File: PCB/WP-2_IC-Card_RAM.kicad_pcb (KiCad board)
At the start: 2 copper layers, 54 x 54 mm, 11 parts, among them J1 Conn_01x38_Female, U1 628128_TSOP-I-32

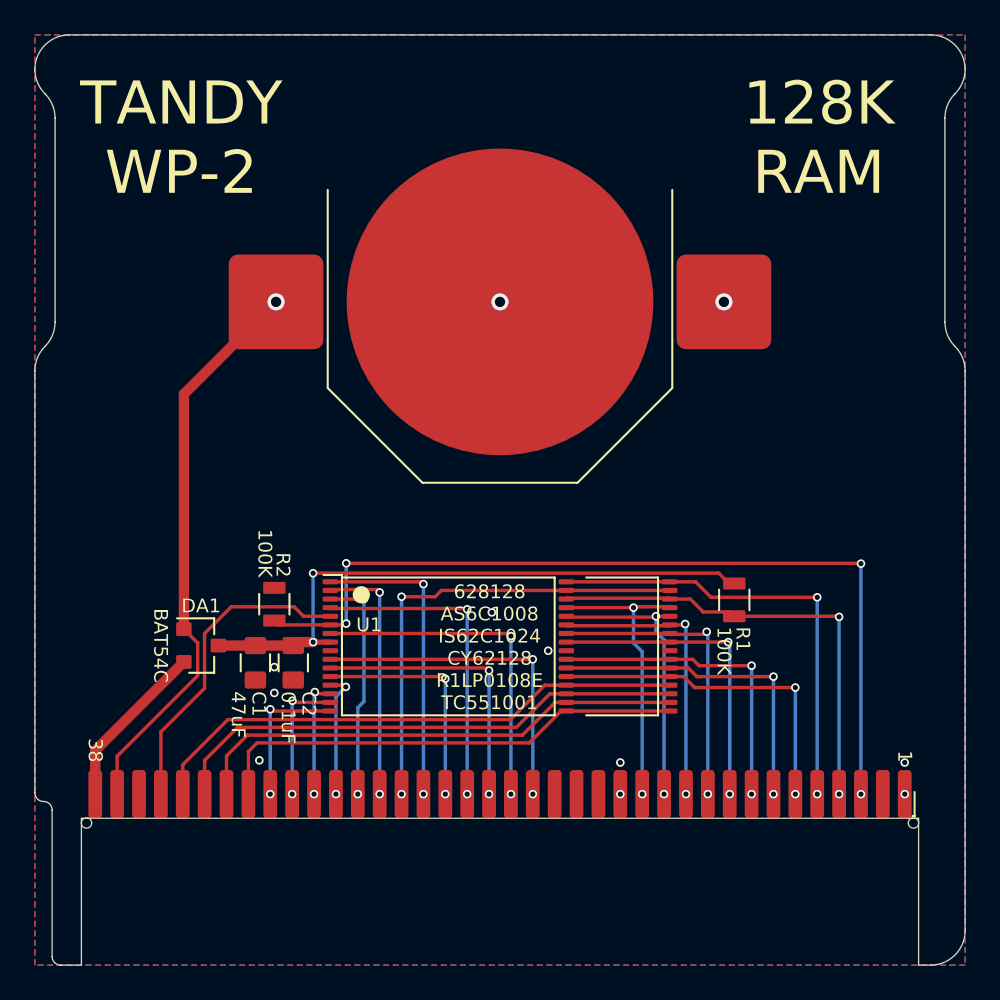
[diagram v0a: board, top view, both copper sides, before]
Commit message: simpler caps for ram card, 3d-printed cover, new WIP 4-bank MRAM card
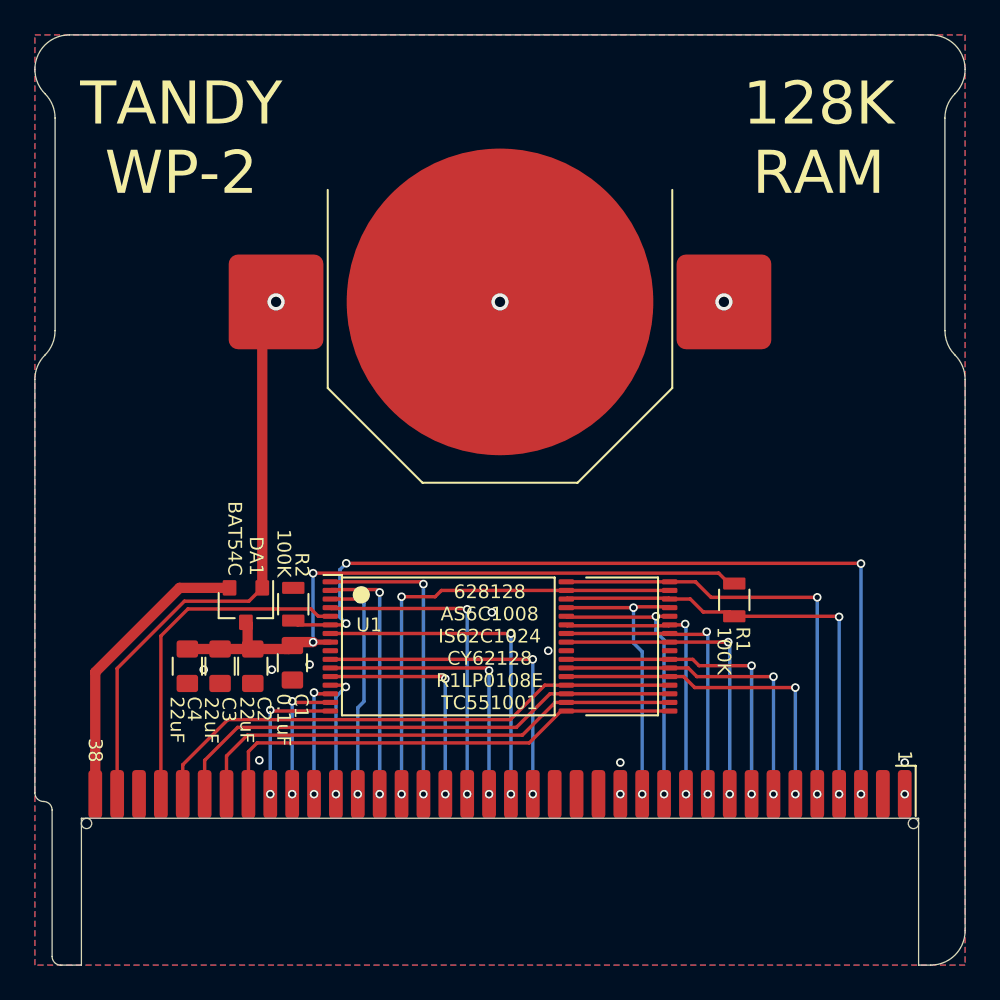
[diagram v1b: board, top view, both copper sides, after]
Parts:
- added C3: 22uF, 0_LOCAL:C_0805_1mm, F.Cu at (119.7, 104.9)
- added C4: 22uF, 0_LOCAL:C_0805_1mm, F.Cu at (117.8, 104.9)
- C1: value 47uF -> 0.1uF; footprint 0_LOCAL:C_0805 -> 0_LOCAL:C_0805_1mm
- C2: value 0.1uF -> 22uF; footprint 0_LOCAL:C_0805 -> 0_LOCAL:C_0805_1mm
- U1: value 628128_TSOP-I-32 -> 628128_TSOP
- moved DA1 3.50 mm to (121.2, 101.3), turned to -90 degrees
- moved C2 2.36 mm to (121.6, 104.9)
- moved C1 2.15 mm to (123.9, 104.7)
- moved R2 1.10 mm to (124.0, 101.3)
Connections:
- net /VMEM renamed VMEM
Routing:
- net /VBUS: track 9.33 -> 16.4 mm
- net VMEM: track 35.3 -> 38.9 mm
- net /VBAT: track 33.1 -> 34.6 mm
- net /~{WE}: track 18.5 -> 19.8 mm
- net /CE2: track 51.1 -> 50.3 mm
- net GND: vias 10 -> 11
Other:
- outline, holes or cut-outs redrawn
- board text added: "Battery: CR2016"
- board text removed: "Battery: CR2016 2 minutes grace period to change battery"

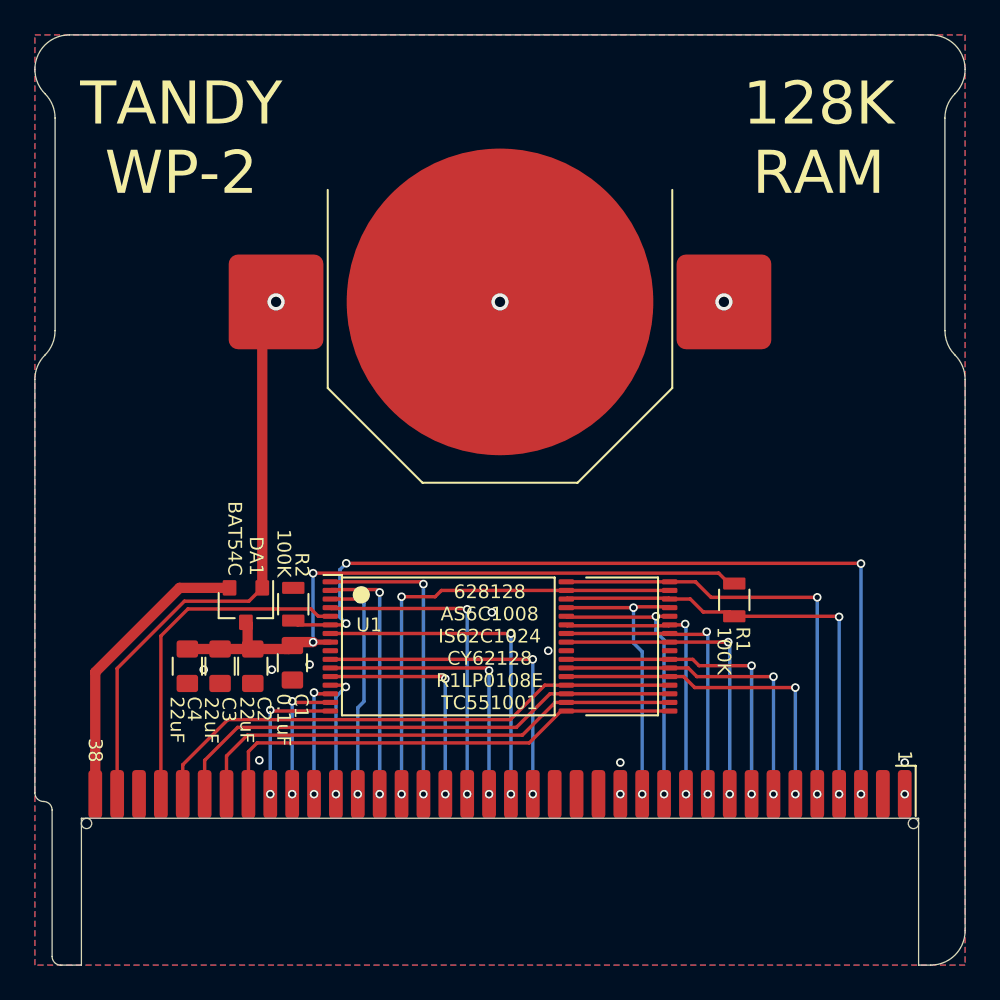
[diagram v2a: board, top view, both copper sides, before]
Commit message: MRAM level shifters, delete FRAM, local datasheets in local symbols
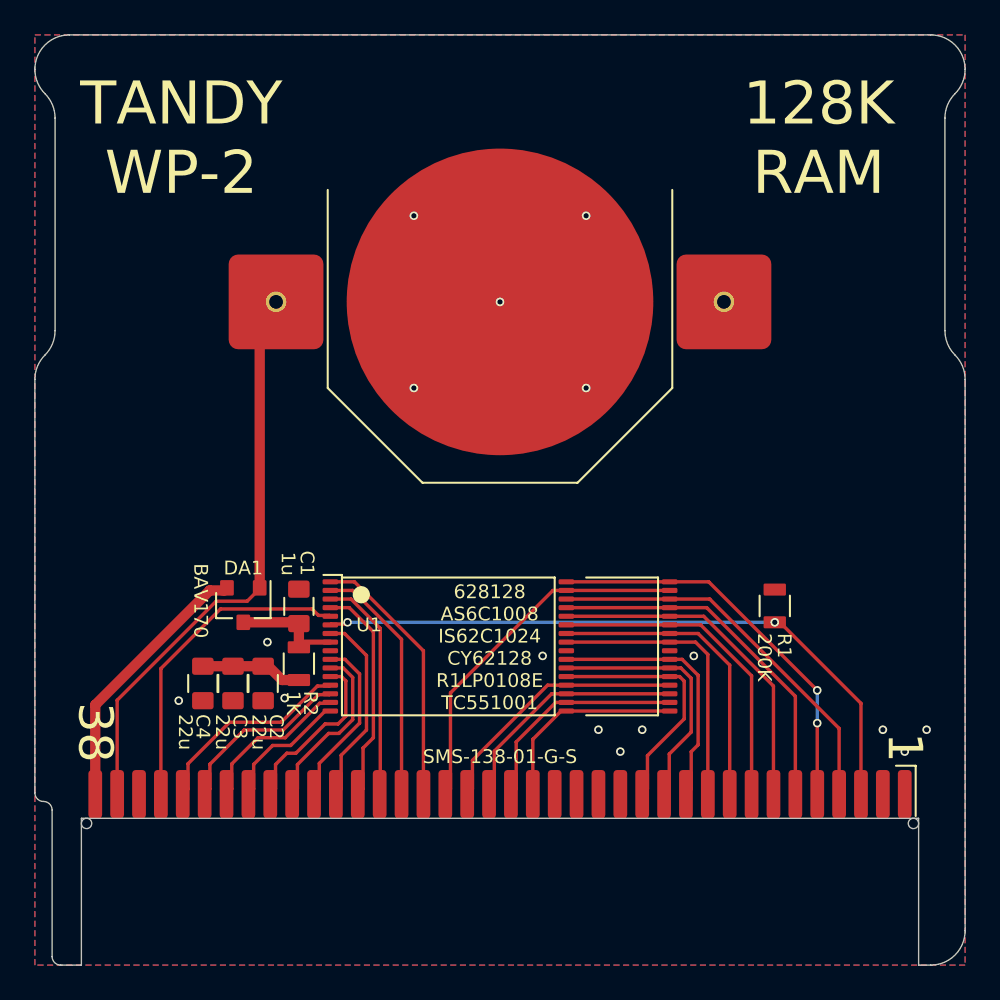
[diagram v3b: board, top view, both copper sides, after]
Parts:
- removed the R1 at (149.6, 101.0)
- added R2: 1K, 0_LOCAL:R_0805, F.Cu at (124.3, 104.7)
- added nail1: pth_nail, 0_LOCAL:pth_nail, F.Cu at (123.0, 83.7)
- added nail2: pth_nail, 0_LOCAL:pth_nail, F.Cu at (148.9, 83.7)
- C1: value 0.1uF -> 1u
- C2, C3, C4: value 22uF -> 22u
- DA1: value BAT54C -> BAV170
- J1: value Conn_01x38_Female -> SMS-138-01-G-S
- R1: renamed from R2; value 100K -> 200K
- moved R1 28.0 mm to (151.9, 101.4)
- moved C1 3.30 mm to (124.3, 101.4), turned to 90 degrees
- moved C4 1.35 mm to (118.7, 105.9)
- moved C3 1.25 mm to (120.5, 105.9)
- moved C2 1.17 mm to (122.2, 105.9)
- moved DA1 0.15 mm to (121.0, 101.3)
- renumbered REF** to corner1, REF** to corner2
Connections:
- C2 pad 1: VMEM -> Net-(C2-Pad1)
- C3 pad 1: VMEM -> Net-(C2-Pad1)
- C4 pad 1: VMEM -> Net-(C2-Pad1)
- U1 pad 10: /A16 -> /A6
- U1 pad 11: /A14 -> /A5
- U1 pad 12: /A12 -> /A4
- U1 pad 13: /A7 -> /A0
- U1 pad 14: /A6 -> /A1
- U1 pad 15: /A5 -> /A2
- U1 pad 16: /A4 -> /A3
- U1 pad 17: /A3 -> /A16
- U1 pad 18: /A2 -> /A15
- U1 pad 19: /A1 -> /A14
- U1 pad 2: /A9 -> /A10
- U1 pad 20: /A0 -> /A13
- U1 pad 21: /D0 -> /D7
- U1 pad 22: /D1 -> /D6
- U1 pad 23: /D2 -> /D5
- U1 pad 25: /D3 -> /D4
- U1 pad 26: /D4 -> /D3
- U1 pad 27: /D5 -> /D2
- U1 pad 28: /D6 -> /D1
- U1 pad 29: /D7 -> /D0
- U1 pad 3: /A8 -> /A9
- U1 pad 31: /A10 -> /A12
- U1 pad 4: /A13 -> /A8
- U1 pad 7: /A15 -> /A7
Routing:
- net VMEM: track 38.9 -> 6.76 mm, vias 2 -> 0
- net /A3: track 27.9 -> 7.59 mm
- net /A2: track 29.2 -> 9.08 mm
- net /A1: track 30.6 -> 10.5 mm
- net /A0: track 31.9 -> 12.0 mm
- net /A10: track 27.2 -> 14.3 mm, vias 2 -> 0
- net /CE2: track 50.3 -> 38.1 mm, vias 4 -> 2
- net /A16: track 19.6 -> 11.8 mm, vias 2 -> 0
- net /A12: track 13.4 -> 21.2 mm, vias 2 -> 0
- net /A15: track 19.8 -> 13.0 mm, vias 2 -> 0
- net Net-(C2-Pad1): track 0.00 -> 5.91 mm
- net /A7: track 7.40 -> 11.4 mm, vias 2 -> 0
- net /~{CE1}: track 26.6 -> 22.8 mm, vias 2 -> 0
- net /A13: track 18.7 -> 15.3 mm, vias 2 -> 0
- net /A6: track 6.87 -> 10.1 mm, vias 2 -> 0
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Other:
- board text removed: "We want plated holes for mechanical strength instead of relying solely on the epoxy under the pads to hold the battery. But we do not want vcc exposed on the bottom surface as it's a shorting risk. The soldermask scratches easily and there is nothing else protecting the pcb. So these vias are customized with no anular ring on the bottom, and no hole in the solder mask on the bottom."

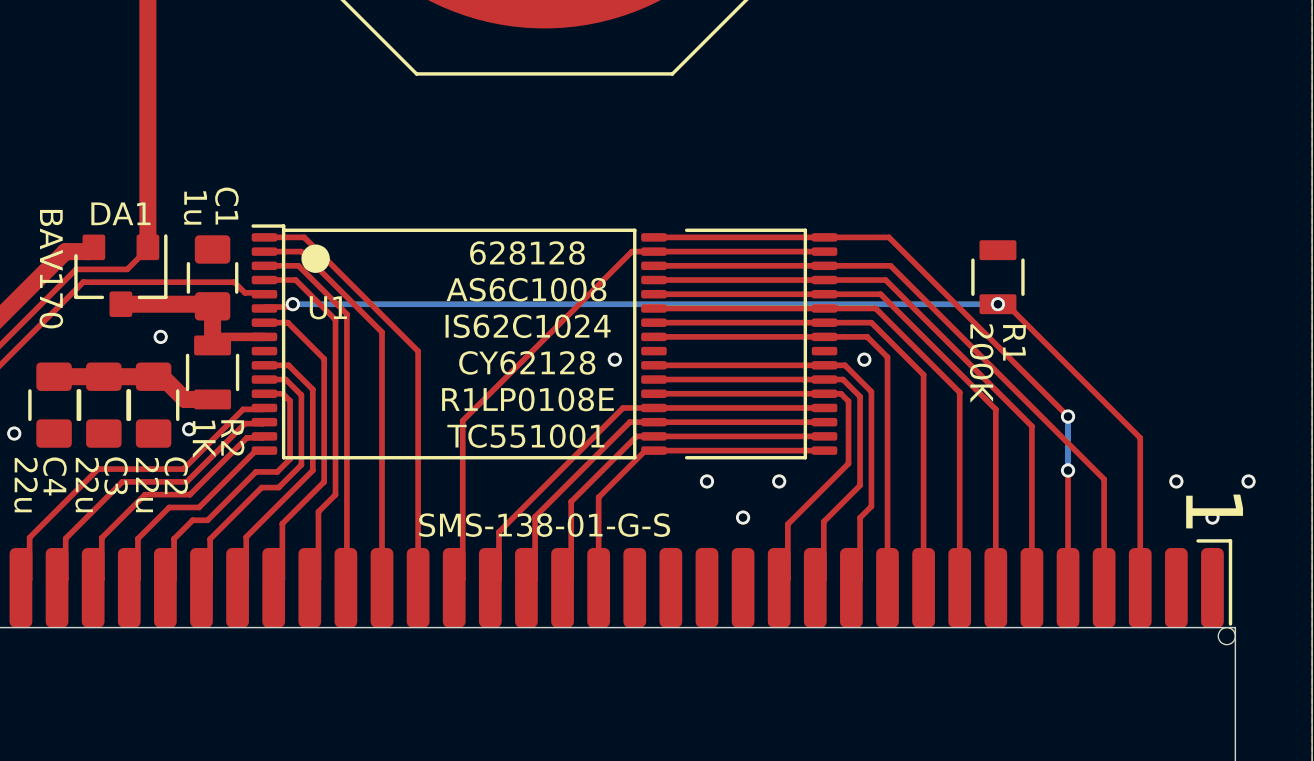
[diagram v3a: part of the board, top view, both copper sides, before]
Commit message: ram 128 move vias off pads and add MPN and fab_bom.csv
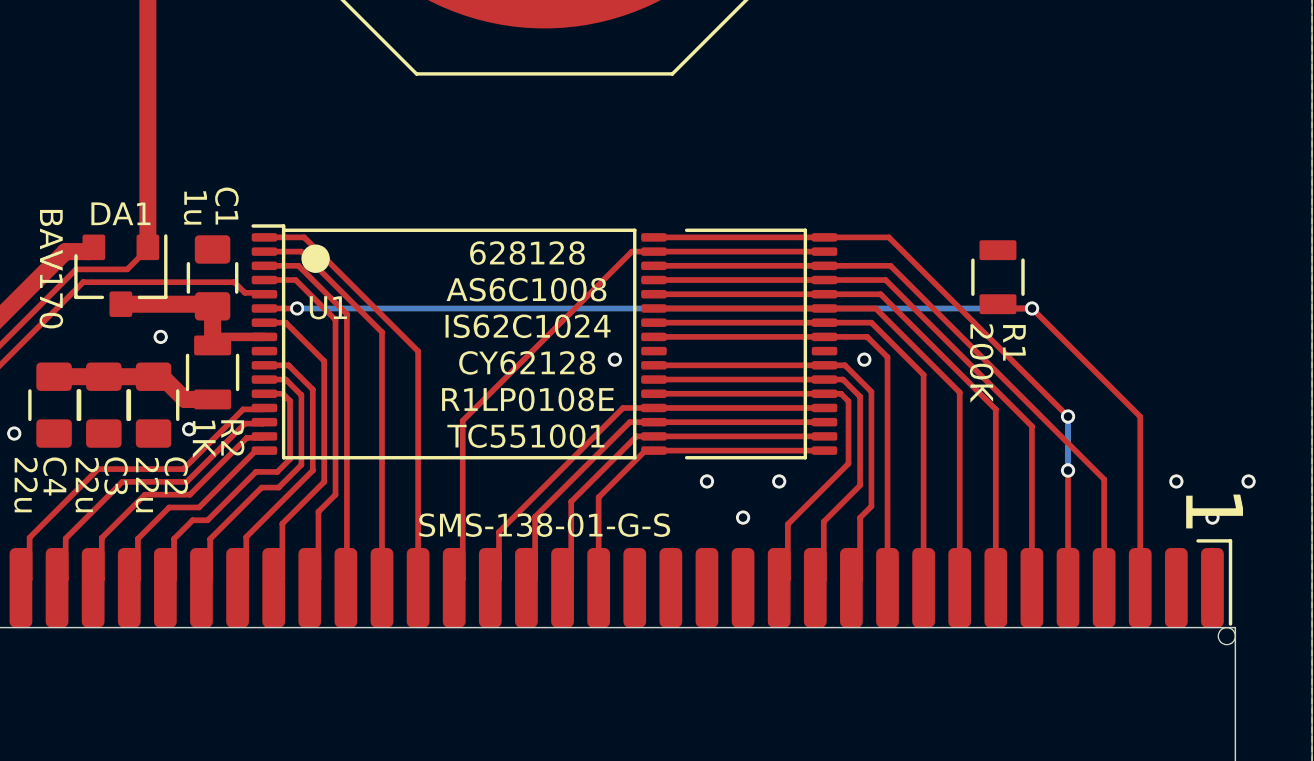
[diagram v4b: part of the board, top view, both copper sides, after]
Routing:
- net /CE2: track 38.1 -> 39.7 mm
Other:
- board text added: "Bottom Soldermask Full Coverage"
- board text added: "PCB THICKNESS 1.2mm ENIG for gold battery contact"
- board text removed: "1.2mm or less PCB thickness. ENIG for gold battery contact."
